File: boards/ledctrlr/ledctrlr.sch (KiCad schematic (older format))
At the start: 66 parts, among them IC1 ATMEGA168-P, IC2 SN75176B, J1 RJ45, J2 RJ45, SW1 SW_PUSH, U1 LM7805, X1 CRYSTAL

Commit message: done with first draft
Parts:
- added PCRNR1, PCRNR2, PCRNR3, PCRNR4: CONN_1, symbol CONN_1
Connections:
- net VCC: no longer JP1.2
- net at C1.1, C2.1, JLGCPWR1.3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: now also JP1.1
- net at C3.1, C4.1, C5.1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: now also C8.1, JP1.2; no longer JP1.1
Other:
- moved on the sheet: PBIGGND1, PLEDVCC1, PLEDVCC2, PLEDVCC3, PLEDVCC4
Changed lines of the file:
@@
-EESchema Schematic File Version 2  date Tue 24 May 2011 09:12:08 PM EDT
+EESchema Schematic File Version 2  date Thu 26 May 2011 09:10:42 PM EDT
 LIBS:power
 LIBS:device
@@
 LIBS:sn75176b
 LIBS:SparkFun
+LIBS:ledctrlr-cache
 EELAYER 24  0
 EELAYER END
@@
 Sheet 1 1
 Title "4-RGB LED Controller Board"
-Date "25 may 2011"
+Date "26 may 2011"
 Rev "1.5"
 Comp "J. Colosimo"
@@
 Comment4 ""
 $EndDescr
-Connection ~ 3050 1850
-Wire Wire Line
-	3050 1950 3050 1650
+$Comp
+L CONN_1 PCRNR4
+U 1 1 4DDEAE72
+P 10000 7200
+F 0 "PCRNR4" H 10050 7200 40  0000 L CNN
+F 1 "CONN_1" H 10000 7255 30  0001 C CNN
+	1    10000 7200
+	1    0    0    -1
+$EndComp
+$Comp
+L CONN_1 PCRNR3
+U 1 1 4DDEAE70
+P 10000 7100
+F 0 "PCRNR3" H 10050 7100 40  0000 L CNN
+F 1 "CONN_1" H 10000 7155 30  0001 C CNN
+	1    10000 7100
+	1    0    0    -1
+$EndComp
+$Comp
+L CONN_1 PCRNR2
+U 1 1 4DDEAE6E
+P 10000 7000
+F 0 "PCRNR2" H 10050 7000 40  0000 L CNN
+F 1 "CONN_1" H 10000 7055 30  0001 C CNN
+	1    10000 7000
+	1    0    0    -1
+$EndComp
+$Comp
+L CONN_1 PCRNR1
+U 1 1 4DDEAE64
+P 10000 6900
+F 0 "PCRNR1" H 10050 6900 40  0000 L CNN
+F 1 "CONN_1" H 10000 6955 30  0001 C CNN
+	1    10000 6900
+	1    0    0    -1
+$EndComp
+Connection ~ 2800 1950
+Wire Wire Line
+	2800 2050 2800 1750
+Connection ~ 2550 1750
+Connection ~ 2800 1850
 Connection ~ 2800 6350
 Wire Wire Line
@@
 Connection ~ 2850 2150
 Wire Wire Line
-	3050 2150 1650 2150
+	3000 2150 1650 2150
 Connection ~ 2550 2150
 Wire Wire Line
@@
 Connection ~ 2300 1750
 Wire Wire Line
-	3050 1750 1650 1750
+	2800 1750 1650 1750
 Connection ~ 1800 1750
 Connection ~ 2700 1550
@@
 Connection ~ 7200 2750
 Wire Wire Line
-	5200 2750 7200 2750
+	7200 2750 5200 2750
 Wire Wire Line
 	5200 4350 5650 4350
@@
 	2300 850  2400 850
 Wire Wire Line
-	3100 2100 2850 2100
-Wire Wire Line
-	2850 2100 2850 1750
-Connection ~ 2850 1750
-Wire Wire Line
 	2950 5750 2950 5850
 Wire Wire Line
@@
 Connection ~ 6600 3750
 Wire Wire Line
-	3700 2100 3700 1050
-Connection ~ 3700 1150
-Wire Wire Line
 	1650 1550 4200 1550
 Connection ~ 3550 1550
@@
 	2400 6850 2950 6850
 Connection ~ 2850 6850
-Connection ~ 3050 1750
+Wire Wire Line
+	3700 1150 3700 1050
+$Comp
+L JUMPER JP1
+U 1 1 4DDD4F59
+P 2300 1450
+F 0 "JP1" H 2300 1600 60  0000 C CNN
+F 1 "JUMPER" H 2300 1370 40  0000 C CNN
+	1    2300 1450
+	0    1    1    0
+$EndComp
 $Comp
 L CONN_1 PLEDVCC2
 U 1 1 4DDC562B
-P 3200 1750
-F 0 "PLEDVCC2" H 3100 1750 40  0000 L CNN
-F 1 "CONN_1" H 3200 1805 30  0001 C CNN
-	1    3200 1750
+P 2950 1850
+F 0 "PLEDVCC2" H 3000 1850 40  0000 L CNN
+F 1 "CONN_1" H 2950 1905 30  0001 C CNN
+	1    2950 1850
 	1    0    0    -1
 $EndComp
@@
 L CONN_1 PLEDVCC4
 U 1 1 4DDC5615
-P 3200 1950
-F 0 "PLEDVCC4" H 3100 1950 40  0000 L CNN
-F 1 "CONN_1" H 3200 2005 30  0001 C CNN
-	1    3200 1950
+P 2950 2050
+F 0 "PLEDVCC4" H 3000 2050 40  0000 L CNN
+F 1 "CONN_1" H 2950 2105 30  0001 C CNN
+	1    2950 2050
 	1    0    0    -1
 $EndComp
@@
 L CONN_1 PLEDVCC3
 U 1 1 4DDC55C5
-P 3200 1850
-F 0 "PLEDVCC3" H 3100 1850 40  0000 L CNN
-F 1 "CONN_1" H 3200 1905 30  0001 C CNN
-	1    3200 1850
+P 2950 1950
+F 0 "PLEDVCC3" H 3000 1950 40  0000 L CNN
+F 1 "CONN_1" H 2950 2005 30  0001 C CNN
+	1    2950 1950
 	1    0    0    -1
 $EndComp
@@
 $EndComp
 $Comp
-L JUMPER JP1
-U 1 1 4DDBFFBF
-P 3400 2100
-F 0 "JP1" H 3600 2050 60  0000 C CNN
-F 1 "JUMPER" H 3400 2020 40  0000 C CNN
-	1    3400 2100
-	1    0    0    -1
-$EndComp
-$Comp
 L C C6
 U 1 1 4DDBFF22
@@
 L CONN_1 PLEDVCC1
 U 1 1 4DDBFD65
-P 3200 1650
-F 0 "PLEDVCC1" H 3100 1650 40  0000 L CNN
-F 1 "CONN_1" H 3200 1705 30  0001 C CNN
-	1    3200 1650
+P 2950 1750
+F 0 "PLEDVCC1" H 3000 1750 40  0000 L CNN
+F 1 "CONN_1" H 2950 1805 30  0001 C CNN
+	1    2950 1750
 	1    0    0    -1
 $EndComp
@@
 L CONN_1 PBIGGND1
 U 1 1 4D34992F
-P 3050 2300
-F 0 "PBIGGND1" V 3100 2250 40  0000 L CNN
-F 1 "CONN_1" H 3050 2355 30  0001 C CNN
-	1    3050 2300
+P 3000 2300
+F 0 "PBIGGND1" V 2900 2450 40  0000 L CNN
+F 1 "CONN_1" H 3000 2355 30  0001 C CNN
+	1    3000 2300
 	0    1    1    0
 $EndComp
@@
 P 2850 2250
 F 0 "#PWR05" H 2850 2300 40  0001 C CNN
-F 1 "GNDPWR" H 2850 2170 40  0000 C CNN
+F 1 "GNDPWR" H 2800 2200 40  0000 C CNN
 	1    2850 2250
 	1    0    0    -1

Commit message: board updates
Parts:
- R1, R6, R7, R8, R9: value 290 -> 1K
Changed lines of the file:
@@
-EESchema Schematic File Version 2  date Thu 26 May 2011 09:10:42 PM EDT
+EESchema Schematic File Version 2  date Wed 01 Jun 2011 04:57:20 PM EDT
 LIBS:power
 LIBS:device
@@
 Sheet 1 1
 Title "4-RGB LED Controller Board"
-Date "26 may 2011"
+Date "1 jun 2011"
 Rev "1.5"
 Comp "J. Colosimo"
@@
 P 6350 3950
 F 0 "R9" V 6430 3950 50  0000 C CNN
-F 1 "290" V 6350 3950 50  0000 C CNN
+F 1 "1K" V 6350 3950 50  0000 C CNN
 	1    6350 3950
 	0    1    1    0
@@
 P 6350 3750
 F 0 "R8" V 6430 3750 50  0000 C CNN
-F 1 "290" V 6350 3750 50  0000 C CNN
+F 1 "1K" V 6350 3750 50  0000 C CNN
 	1    6350 3750
 	0    1    1    0
@@
 P 6350 3550
 F 0 "R7" V 6430 3550 50  0000 C CNN
-F 1 "290" V 6350 3550 50  0000 C CNN
+F 1 "1K" V 6350 3550 50  0000 C CNN
 	1    6350 3550
 	0    1    1    0
@@
 P 6350 3350
 F 0 "R6" V 6430 3350 50  0000 C CNN
-F 1 "290" V 6350 3350 50  0000 C CNN
+F 1 "1K" V 6350 3350 50  0000 C CNN
 	1    6350 3350
 	0    1    1    0
@@
 P 4200 1300
 F 0 "R1" V 4280 1300 50  0000 C CNN
-F 1 "290" V 4200 1300 50  0000 C CNN
+F 1 "1K" V 4200 1300 50  0000 C CNN
 	1    4200 1300
 	1    0    0    -1

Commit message: added ground plane, exported gerbers, etc., created export folder
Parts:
- C1, C4: footprint (none) -> C1; DigikeyPart (none) -> 478-5812-ND; Part (none) -> TAP105M035SCS
- C10, C11: value 22pF -> 8pF; footprint (none) -> SM0805; DigikeyPart (none) -> 311-1097-1-ND; Part (none) -> CC0805DRNP09BN8R0
- C2, C6, C7, C8: footprint (none) -> C1; DigikeyPart (none) -> 478-4862-ND; Part (none) -> SR215C103KAR
- C3: footprint (none) -> Elko_vert_DM7-5_RM2-5; DigikeyPart (none) -> P5137-ND; Part (none) -> ECA-1CM470
- C5: footprint (none) -> C1; DigikeyPart (none) -> 478-1831-ND; Part (none) -> TAP104K035SCS
- C9: footprint (none) -> SM0805; DigikeyPart (none) -> 08055C104KAT2A; Part (none) -> 478-1395-1-ND
- D1: footprint (none) -> LED-1206; DigikeyPart (none) -> 754-1142-1-ND; Part (none) -> APT3216SRCPRV
- D2, D3, D4, D5: footprint (none) -> LED-1206; DigikeyPart (none) -> 754-1141-1-ND; Part (none) -> APT3216SGC
- IC1: footprint DIL28 -> DIP-28__300; DigikeyPart (none) -> ATMEGA168-20PU-ND; Part (none) -> ATMEGA168-20PU
- IC2: footprint DIL8 -> DIP-8__300; DigikeyPart (none) -> 296-1739-5-ND; Part (none) -> SN75176BP
- J1, J2: footprint (none) -> RJ45_8; DigikeyPart (none) -> WM5572-ND; Part (none) -> 95501-2882
- JLEDPWR2, JLGCPWR1: footprint (none) -> JACK_ALIM; DigikeyPart (none) -> CP-202A-ND; Part (none) -> PJ-202A
- JP1: footprint (none) -> SM1206; DigikeyPart (none) -> N/A; Part (none) -> N/A
- JP2: footprint (none) -> 1206; DigikeyPart (none) -> N/A; Part (none) -> N/A
- PBIGGND1, PCRNR1, PCRNR2, PCRNR3, PCRNR4, PLEDB0, PLEDB1, PLEDB2, PLEDB3, PLEDB4, PLEDG0, PLEDG1, PLEDG2, PLEDG3, PLEDG4, PLEDR0, PLEDR1, PLEDR2, PLEDR3, PLEDR4: footprint (none) -> 1pin; DigikeyPart (none) -> N/A; Part (none) -> N/A
- PLEDVCC1, PLEDVCC2, PLEDVCC3, PLEDVCC4, PSOUT1, PX1, PX2, PX3, PX4, PX5: footprint (none) -> SIL-1; DigikeyPart (none) -> N/A; Part (none) -> N/A
- R1, R6, R7, R8, R9: footprint (none) -> SM0805; DigikeyPart (none) -> RMCF0805JT1K00CT-ND; Part (none) -> RMCF0805JT1K00
- R10: footprint (none) -> SM0805; DigikeyPart (none) -> RMCF0805JT120RCT-ND; Part (none) -> RMCF0805JT120R
- R2: footprint (none) -> SM0805; DigikeyPart (none) -> RMCF0805JT10K0CT-ND; Part (none) -> RMCF0805JT10K0
- R3, R4, R5: footprint (none) -> SM0805; DigikeyPart (none) -> RMCF0805JT330RCT-ND; Part (none) -> RMCF0805JT330R
- SW1: footprint (none) -> PUSH_SW; DigikeyPart (none) -> 450-1662-ND; Part (none) -> FSMRA2JH
- TLC1, TLC2, TLC3: footprint (none) -> DIP-28__300; DigikeyPart (none) -> 296-17732-5-ND; Part (none) -> TLC5940NT
- U1: footprint (none) -> LM78XXV; DigikeyPart (none) -> LM7805CT-ND; Part (none) -> LM7805CT
- X1: footprint (none) -> SM1206; DigikeyPart (none) -> 644-1026-1-ND; Part (none) -> NX8045GB-20.000000MHZ

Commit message: fixed regular board, added mini board
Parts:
- X1: footprint SM1206 -> Crystal_FOX-FE-SMD-RevA_09Aug201
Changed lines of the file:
@@
-EESchema Schematic File Version 2  date Tue 14 Jun 2011 12:07:09 AM EDT
+EESchema Schematic File Version 2  date Sun 17 Jul 2011 11:37:49 AM EDT
 LIBS:power
 LIBS:device
@@
 Sheet 1 1
 Title "4-RGB LED Controller Board"
-Date "14 jun 2011"
+Date "17 jul 2011"
 Rev "1.5"
 Comp "J. Colosimo"
@@
 F 0 "X1" H 4650 2300 60  0000 C CNN
 F 1 "CRYSTAL" H 4650 2000 60  0000 C CNN
-F 2 "SM1206" H 4590 2360 60  0001 C CNN
+F 2 "Crystal_FOX-FE-SMD-RevA_09Aug201" H 4590 2360 60  0001 C CNN
 F 4 "NX8045GB-20.000000MHZ" H 4650 2150 60  0001 C CNN "Part"
 F 5 "644-1026-1-ND" H 4650 2150 60  0001 C CNN "DigikeyPart"

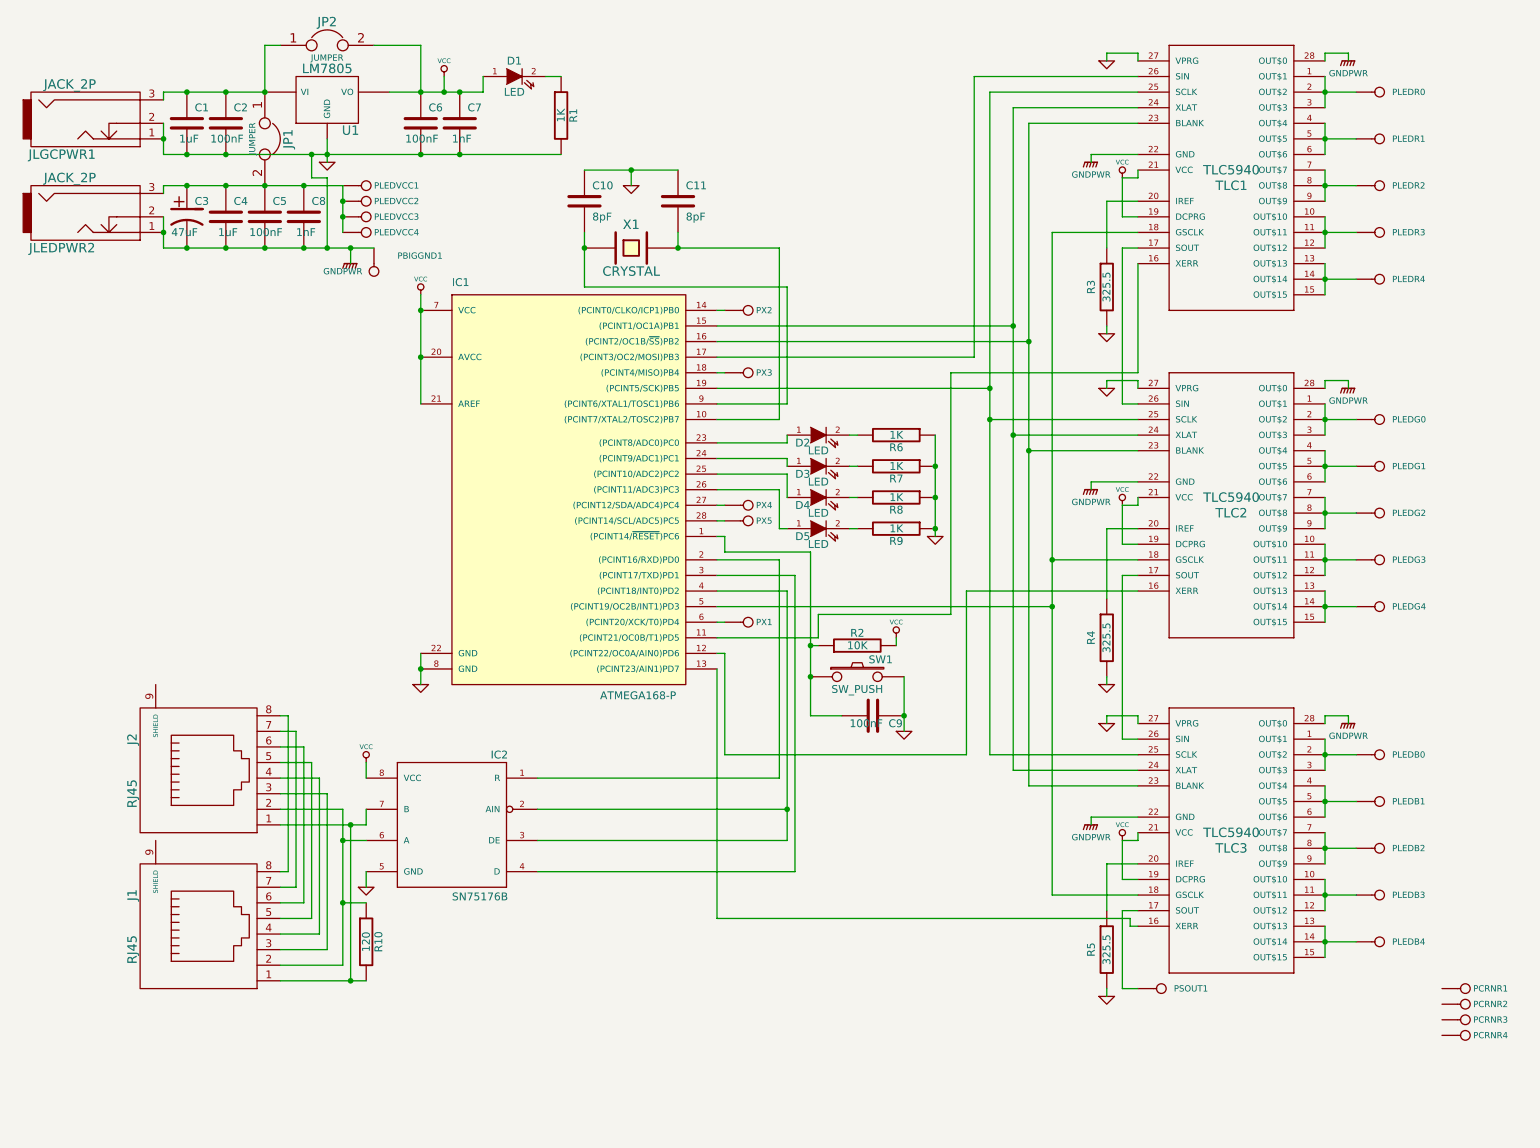
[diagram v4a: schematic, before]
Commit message: ignore .*
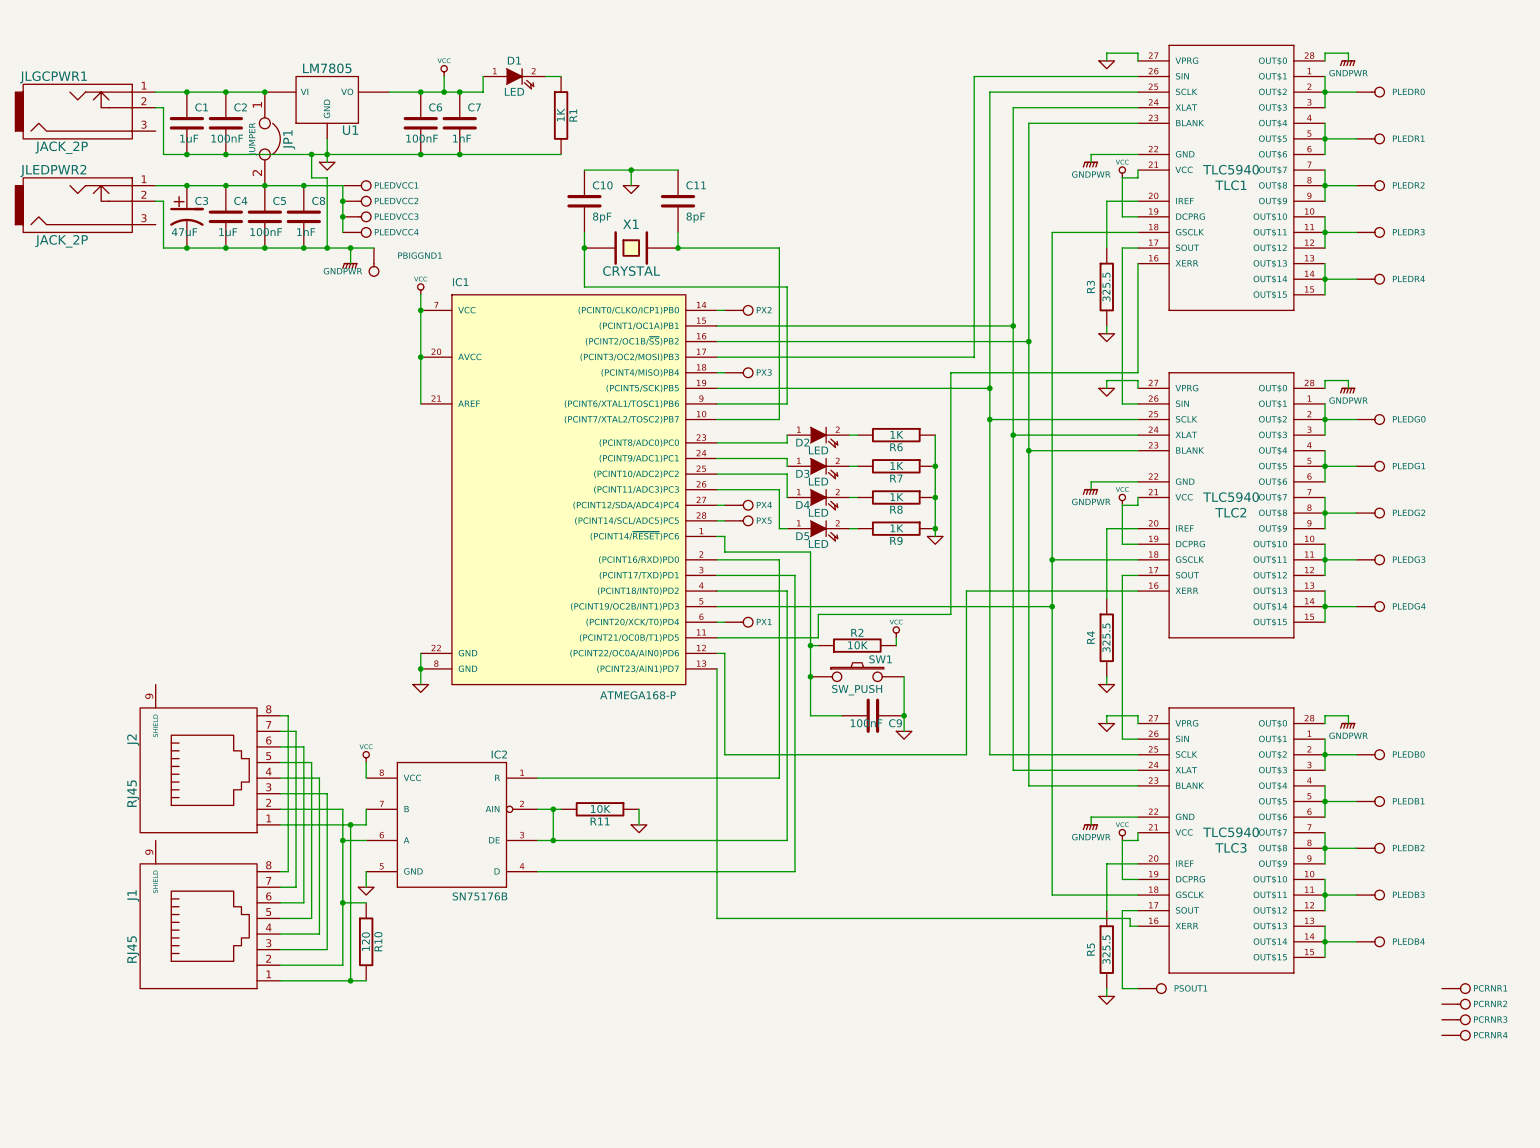
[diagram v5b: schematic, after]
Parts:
- removed JP2: JUMPER, 1206, symbol JUMPER
- added R11: 10K, symbol R
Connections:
- net GND: now also R11.1; no longer JLEDPWR2.1, JLGCPWR1.1
- net at IC1.4 ((PCINT18/INT0)PD2), IC2.2 (AIN), IC2.3 (DE): now also R11.2
- net at C1.1, C2.1, JP1.1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: now also JLGCPWR1.1; no longer JLGCPWR1.3
- net at C3.1, C4.1, C5.1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: now also JLEDPWR2.1; no longer JLEDPWR2.3
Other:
- moved on the sheet: JLEDPWR2, JLGCPWR1

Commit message: added screw terminals, no work done
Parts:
- removed PLEDB0, PLEDB1, PLEDB2, PLEDB3, PLEDB4, PLEDG0, PLEDG1, PLEDG2, PLEDG3, PLEDG4, PLEDR0, PLEDR1, PLEDR2, PLEDR3, PLEDR4: CONN_1, 1pin, symbol CONN_1
- removed PLEDVCC1, PLEDVCC2, PLEDVCC3, PLEDVCC4: CONN_1, SIL-1, symbol CONN_1
- added K1: CONN_4, OSTTA040161, symbol CONN_4
- added K2: CONN_12, OSTTA120161, symbol CONN_12
- added K3: CONN_3, OSTTA030161, symbol CONN_3
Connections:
- net at TLC1.1 (OUT$1), TLC1.2 (OUT$2), TLC1.3 (OUT$3): now also K2.1 (P1)
- net at TLC1.10 (OUT$10), TLC1.11 (OUT$11), TLC1.12 (OUT$12): now also K2.4 (P4)
- net at TLC1.13 (OUT$13), TLC1.14 (OUT$14), TLC1.15 (OUT$15): now also K2.5 (P5)
- net at TLC1.4 (OUT$4), TLC1.5 (OUT$5), TLC1.6 (OUT$6): now also K2.2 (P2)
- net at TLC1.7 (OUT$7), TLC1.8 (OUT$8), TLC1.9 (OUT$9): now also K2.3 (P3)
- net at TLC2.1 (OUT$1), TLC2.2 (OUT$2), TLC2.3 (OUT$3): now also K2.6 (P6)
- net at TLC2.10 (OUT$10), TLC2.11 (OUT$11), TLC2.12 (OUT$12): now also K2.9 (P9)
- net at TLC2.13 (OUT$13), TLC2.14 (OUT$14), TLC2.15 (OUT$15): now also K2.10 (P10)
- net at TLC2.4 (OUT$4), TLC2.5 (OUT$5), TLC2.6 (OUT$6): now also K2.7 (P7)
- net at TLC2.7 (OUT$7), TLC2.8 (OUT$8), TLC2.9 (OUT$9): now also K2.8 (P8)
- net at TLC3.1 (OUT$1), TLC3.2 (OUT$2), TLC3.3 (OUT$3): now also K2.11 (P11)
- net at TLC3.10 (OUT$10), TLC3.11 (OUT$11), TLC3.12 (OUT$12): now also K3.2 (PM)
- net at TLC3.13 (OUT$13), TLC3.14 (OUT$14), TLC3.15 (OUT$15): now also K3.3 (P3)
- net at TLC3.4 (OUT$4), TLC3.5 (OUT$5), TLC3.6 (OUT$6): now also K2.12 (P12)
- net at TLC3.7 (OUT$7), TLC3.8 (OUT$8), TLC3.9 (OUT$9): now also K3.1 (P1)
- net at C3.1, C4.1, C5.1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: now also K1.1 (P1), K1.2 (P2), K1.3 (P3), K1.4 (P4)

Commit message: working on new version
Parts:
- removed K1: CONN_4, OSTTA040161, symbol CONN_4
- removed K2: CONN_12, OSTTA120161, symbol CONN_12
- removed K3: CONN_3, OSTTA030161, symbol CONN_3
- added LED0, LED1, LED2, LED3, LED4: CONN_4, symbol CONN_4
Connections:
- net LEDRED0: now reaches TLC1.1 (OUT$1), TLC1.2 (OUT$2), TLC1.3 (OUT$3)
- net LEDRED0: now also LED0.2 (P2)
- net LEDRED3: now reaches TLC1.10 (OUT$10), TLC1.11 (OUT$11), TLC1.12 (OUT$12)
- net LEDRED3: now also LED3.2 (P2)
- net LEDRED4: now reaches TLC1.13 (OUT$13), TLC1.14 (OUT$14), TLC1.15 (OUT$15)
- net LEDRED4: now also LED4.2 (P2)
- net LEDRED1: now reaches TLC1.4 (OUT$4), TLC1.5 (OUT$5), TLC1.6 (OUT$6)
- net LEDRED1: now also LED1.2 (P2)
- net LEDRED2: now reaches TLC1.7 (OUT$7), TLC1.8 (OUT$8), TLC1.9 (OUT$9)
- net LEDRED2: now also LED2.2 (P2)
- net LEDGRN0: now reaches TLC2.1 (OUT$1), TLC2.2 (OUT$2), TLC2.3 (OUT$3)
- net LEDGRN0: now also LED0.3 (P3)
- net LEDGRN3: now reaches TLC2.10 (OUT$10), TLC2.11 (OUT$11), TLC2.12 (OUT$12)
- net LEDGRN3: now also LED3.3 (P3)
- net LEDGRN4: now reaches TLC2.13 (OUT$13), TLC2.14 (OUT$14), TLC2.15 (OUT$15)
- net LEDGRN4: now also LED4.3 (P3)
- net LEDGRN1: now reaches TLC2.4 (OUT$4), TLC2.5 (OUT$5), TLC2.6 (OUT$6)
- net LEDGRN1: now also LED1.3 (P3)
- net LEDGRN2: now reaches TLC2.7 (OUT$7), TLC2.8 (OUT$8), TLC2.9 (OUT$9)
- net LEDGRN2: now also LED2.3 (P3)
- net LEDBLU0: now reaches TLC3.1 (OUT$1), TLC3.2 (OUT$2), TLC3.3 (OUT$3)
- net LEDBLU0: now also LED0.4 (P4)
- net LEDBLU3: now reaches TLC3.10 (OUT$10), TLC3.11 (OUT$11), TLC3.12 (OUT$12)
- net LEDBLU3: now also LED3.4 (P4)
- net LEDBLU4: now reaches TLC3.13 (OUT$13), TLC3.14 (OUT$14), TLC3.15 (OUT$15)
- net LEDBLU4: now also LED4.4 (P4)
- net LEDBLU1: now reaches TLC3.4 (OUT$4), TLC3.5 (OUT$5), TLC3.6 (OUT$6)
- net LEDBLU1: now also LED1.4 (P4)
- net LEDBLU2: now reaches TLC3.7 (OUT$7), TLC3.8 (OUT$8), TLC3.9 (OUT$9)
- net LEDBLU2: now also LED2.4 (P4)
- net VAA: now reaches C3.1, C4.1, C5.1, C8.1, JLEDPWR2.1, JP1.2
- net VAA: now also LED0.1 (P1), LED1.1 (P1), LED2.1 (P1), LED3.1 (P1), LED4.1 (P1)
- no-connect marks 0 -> 6
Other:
- moved on the sheet: C1, C10, C11, C2, C3, C4, C5, C6, C7, C8, C9, D1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
